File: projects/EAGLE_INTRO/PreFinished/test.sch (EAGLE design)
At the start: 5 parts

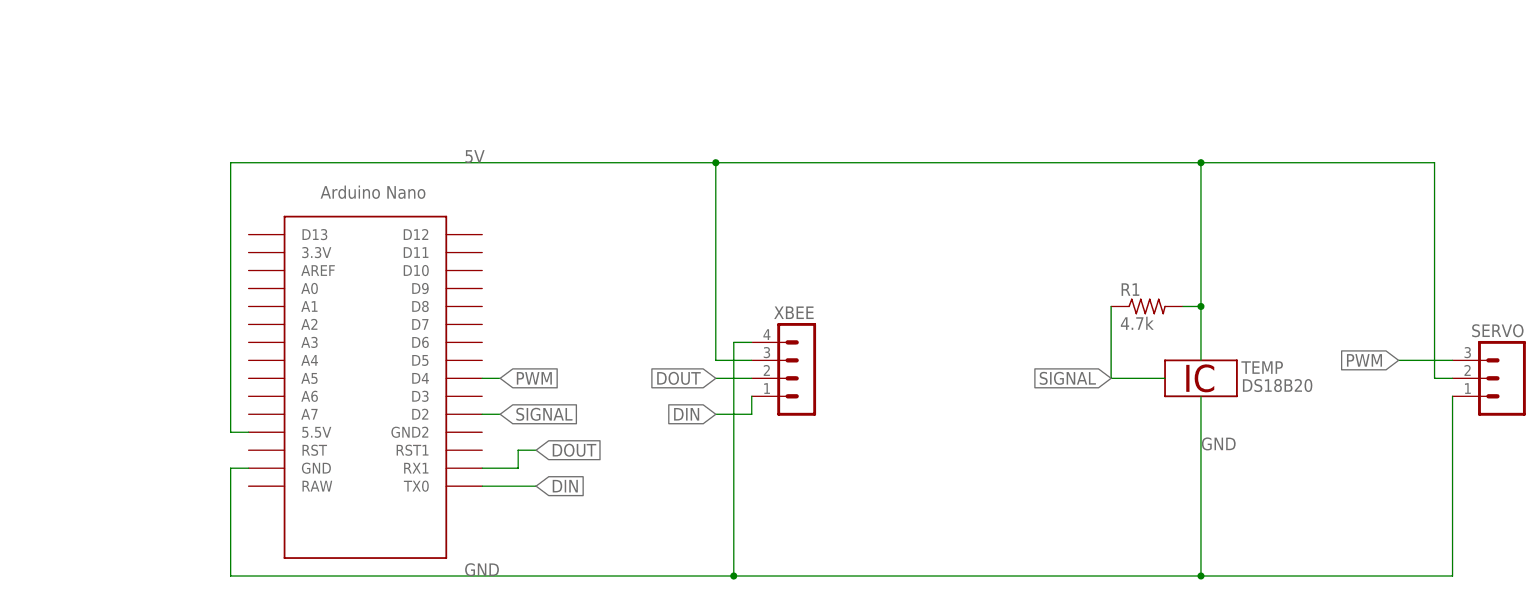
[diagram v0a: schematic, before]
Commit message: Added edits to teensy 3.6 schematic for the plantower. Added stuff from EAGLE intro presentation.
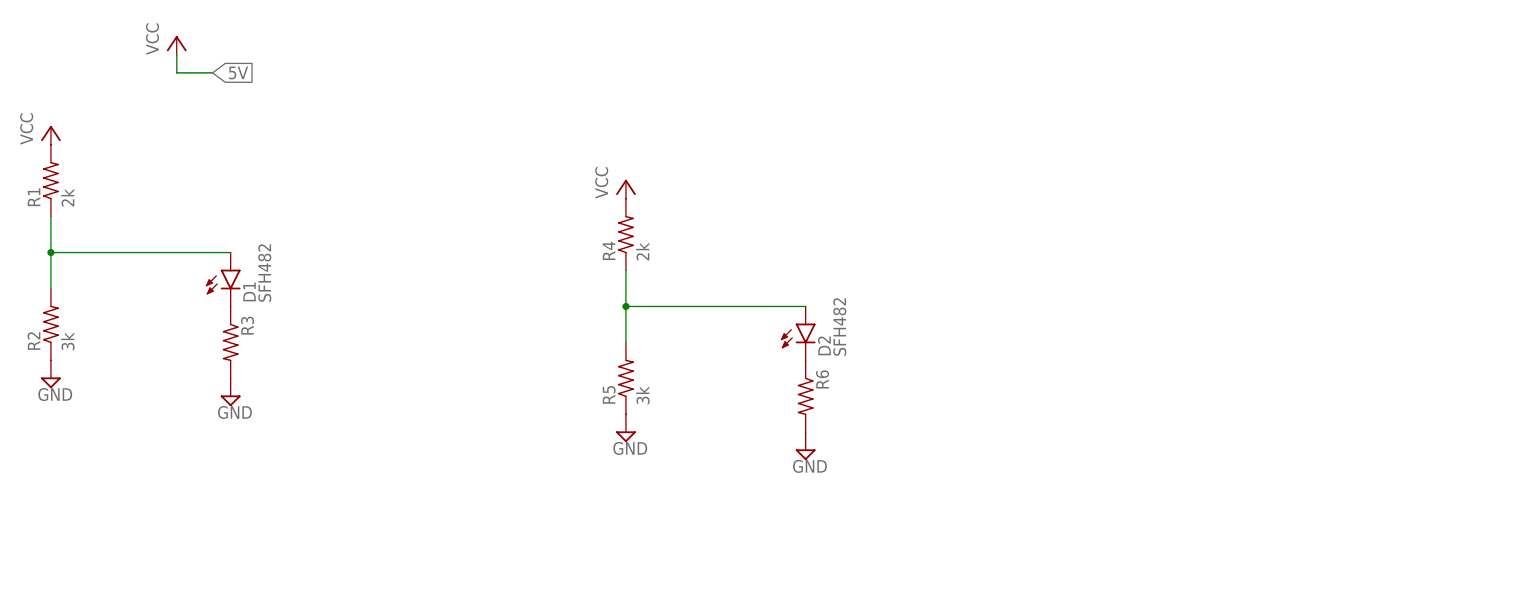
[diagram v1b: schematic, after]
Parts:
- removed SERVO: (no value), con-amp-quick:M03
- removed TEMP: DS18B20, 1wire:DS18B20
- removed U$1: NANO, Arduino-clone:NANO
- removed XBEE: (no value), con-lstb:MA04-1
- added D1, D2: SFH482, led:SFH482
- added R2, R5: 3k, rcl:R-US_0204/7
- added R3, R6: (no value), rcl:R-US_0204/7
- added R4: 2k, rcl:R-US_0204/7
- R1: value 4.7k -> 2k; device resistor:R-US_0204/7 -> rcl:R-US_0204/7
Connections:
- removed net 5V: R1.2, SERVO.2, U$1.5.5V, XBEE.3
- removed net DIN: U$1.TX0, XBEE.1
- removed net DOUT: U$1.RX1, XBEE.2
- removed net PWM: SERVO.3, U$1.D4
- removed net SIGNAL: R1.1, U$1.D2
- new net N$1: D1.C, R3.1
- new net N$2: D1.A, R1.1, R2.2
- new net N$3: D2.C, R6.1
- new net N$4: D2.A, R4.1, R5.2
- new net VCC: R1.2, R4.2
- net GND: now also R2.1, R3.2, R5.1, R6.2; no longer SERVO.1, U$1.GND, XBEE.4
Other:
- moved on the sheet: R1
